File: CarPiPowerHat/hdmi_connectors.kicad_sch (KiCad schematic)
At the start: 3 parts, among them J1 690-019-298-412, J2 690-019-298-412, J6 Conn_01x15_Female

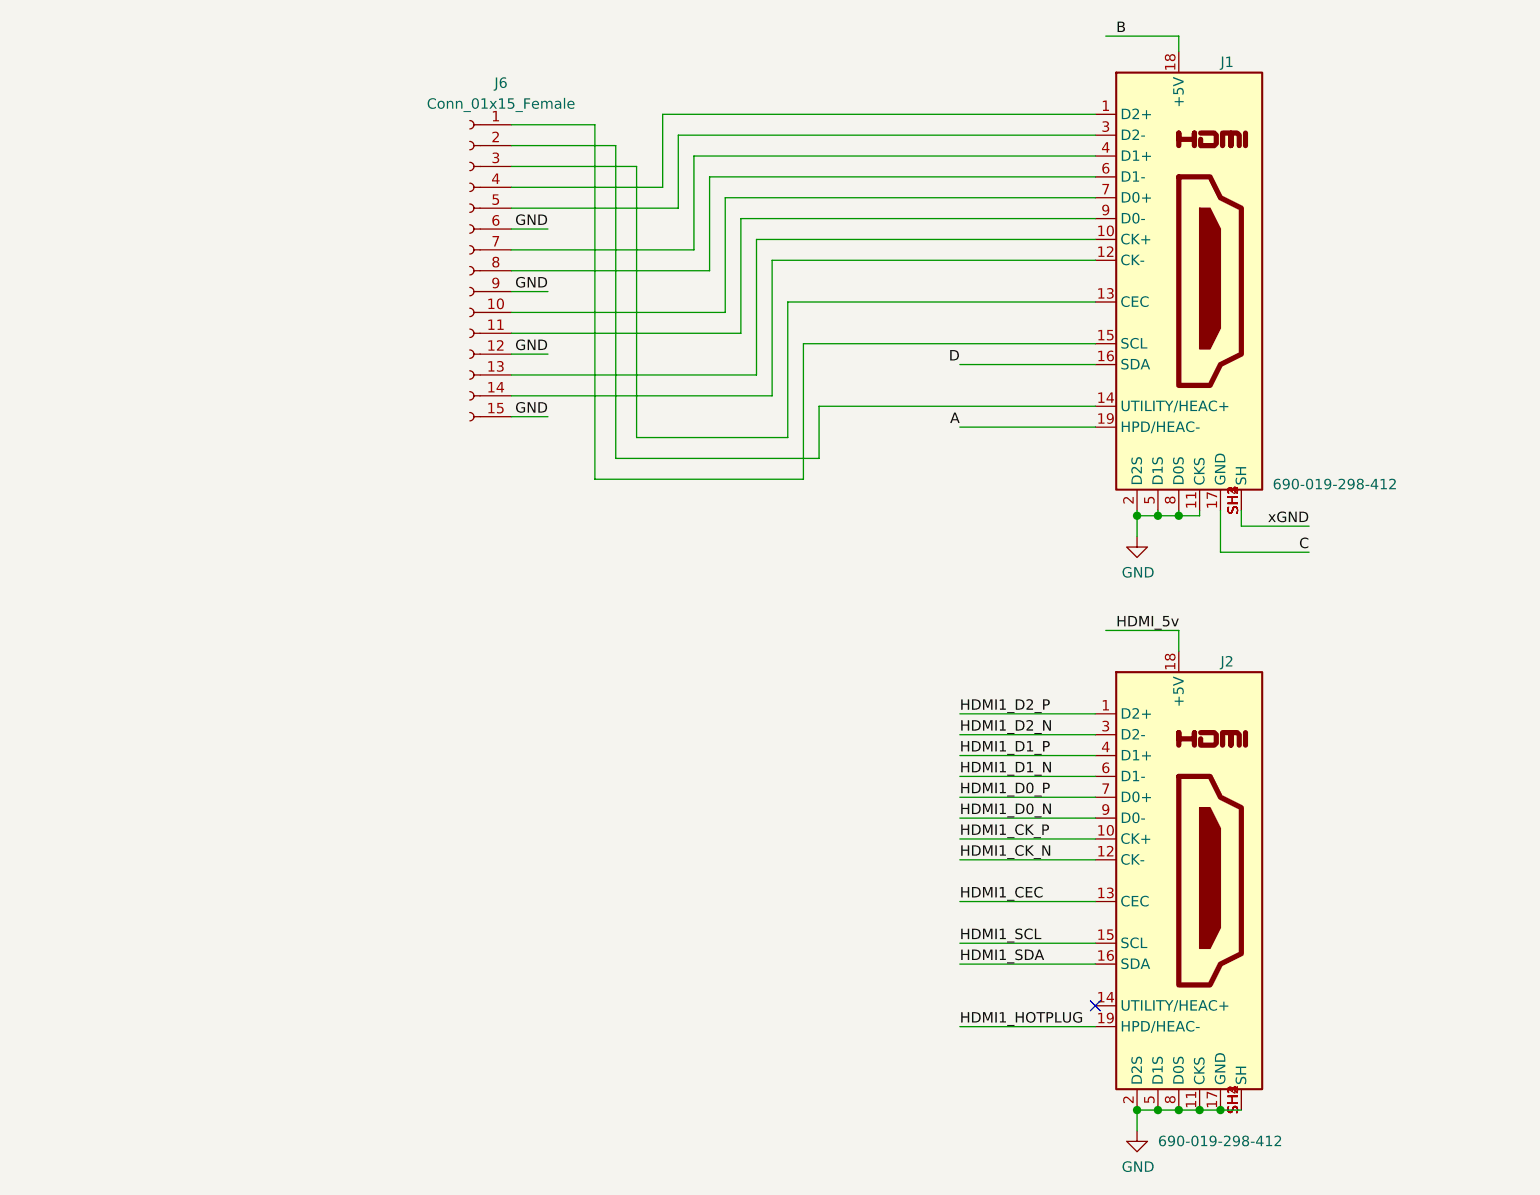
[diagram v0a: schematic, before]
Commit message: added connectors
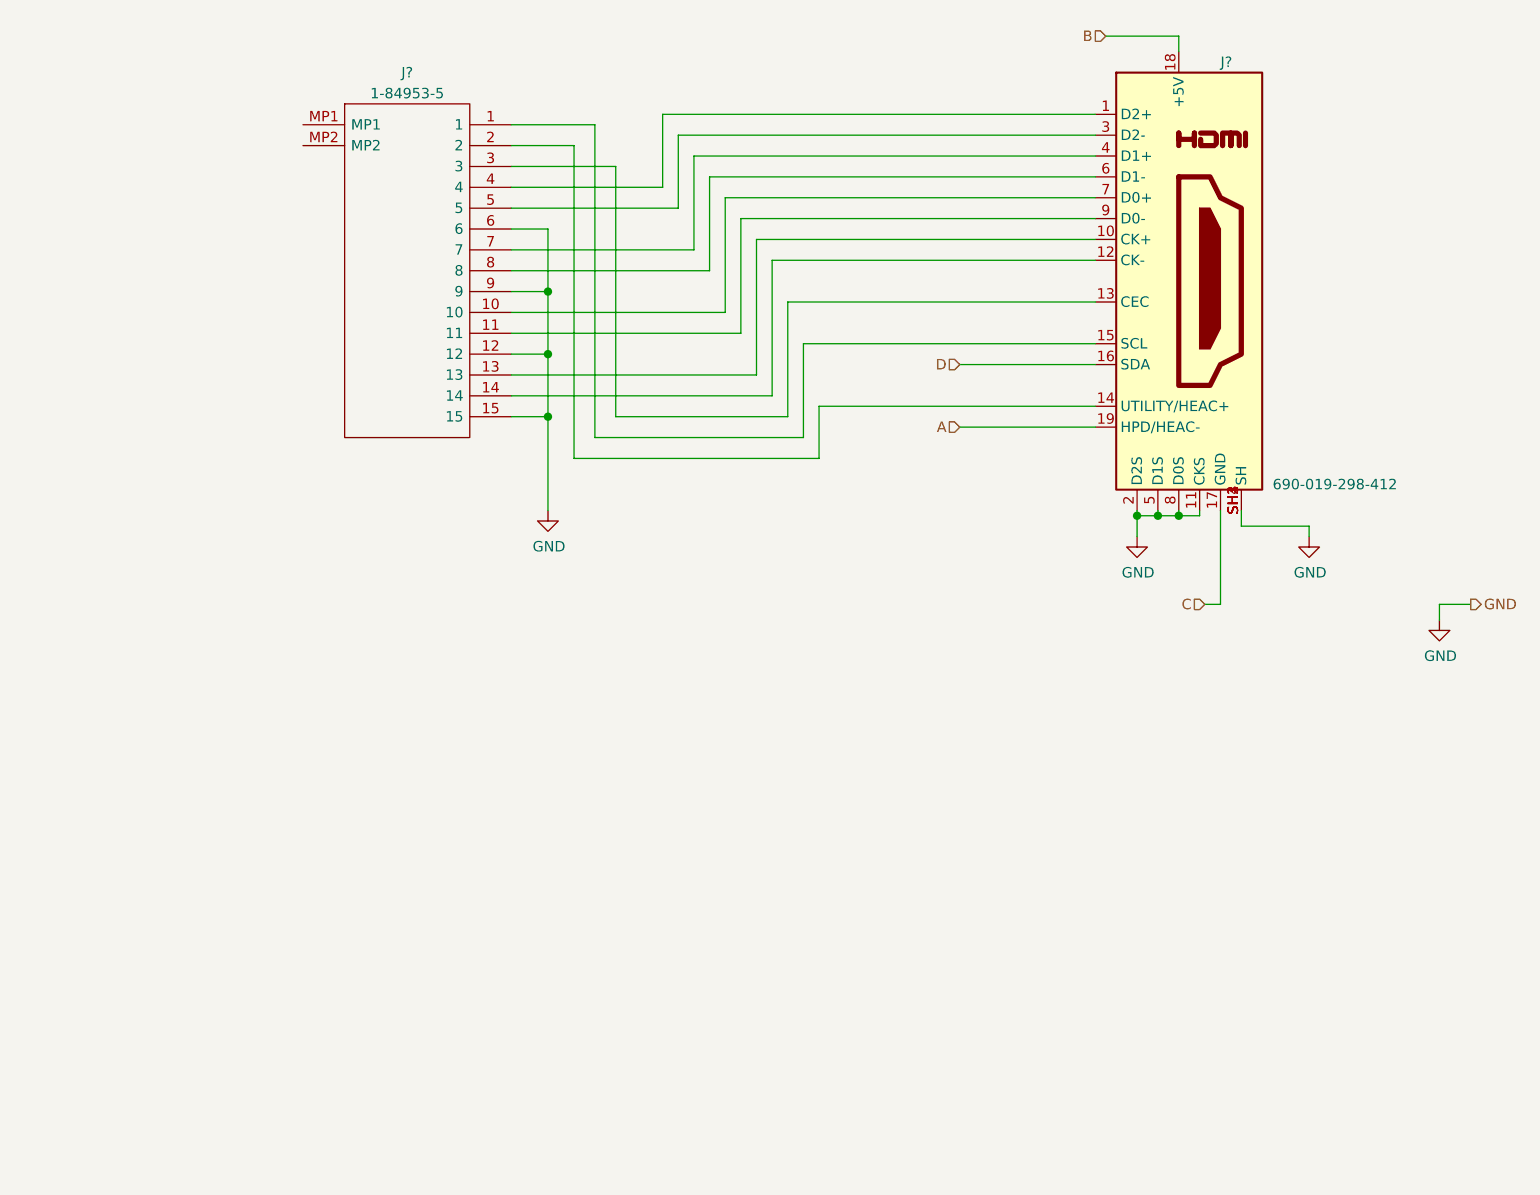
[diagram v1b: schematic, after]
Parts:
- removed J2: 690-019-298-412, project_footprints:EDAC 690-019-298-412, symbol CM4IO:HDMI_A_1.4
- removed J6: Conn_01x15_Female, symbol Connector:Conn_01x15_Female
- added J?: 1-84953-5, project_footprints:1849535, symbol 1-84953-5:1-84953-5
- renumbered J1 to J?
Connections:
- net xGND is gone; now on net GND: J?.SH1 (SH), J?.SH2 (SH), J?.SH3 (SH), J?.SH4 (SH)
- net GND: now also J?.12, J?.15, J?.6, J?.9
- net at J?.15 (SCL): now also J?.1
- net at J?.7 (D0+): now also J?.10
- net at J?.9 (D0-): now also J?.11
- net at J?.10 (CK+): now also J?.13
- net at J?.12 (CK-): now also J?.14
- net at J?.14 (UTILITY/HEAC+): now also J?.2
- net at J?.13 (CEC): now also J?.3
- net at J?.1 (D2+): now also J?.4
- net at J?.3 (D2-): now also J?.5
- net at J?.4 (D1+): now also J?.7
- net at J?.6 (D1-): now also J?.8
- no-connect marks 1 -> 0

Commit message: doing some traces
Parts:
- J7: renamed from J?; value 690-019-298-412 -> HDMI_A_1.4; symbol CM4IO:HDMI_A_1.4 -> CarPiPowerHat:HDMI_A_1.4
- gave numbers to parts that had none: 1
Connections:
- net D2+: now reaches J2.4, J7.1 (D2+)
- net CK+: now reaches J2.13, J7.10 (CK+)
- net CK-: now reaches J2.14, J7.12 (CK-)
- net CEC: now reaches J2.3, J7.13 (CEC)
- net UTILITY/HEAC+: now reaches J2.2, J7.14 (UTILITY/HEAC+)
- net C_SCL: now reaches J2.1, J7.15 (SCL)
- net D2-: now reaches J2.5, J7.3 (D2-)
- net D1-: now reaches J2.7, J7.4 (D1+)
- net D1+: now reaches J2.8, J7.6 (D1-)
- net D0+: now reaches J2.10, J7.7 (D0+)
- net D0-: now reaches J2.11, J7.9 (D0-)
- no-connect marks 0 -> 2
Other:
- moved on the sheet: J2
